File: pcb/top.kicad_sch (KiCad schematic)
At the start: 64 parts, among them J1 Conn_01x01, J10 Conn_01x01, J11 Conn_01x01, J2 Conn_01x01, J3 Conn_01x06, J4 Conn_01x01, J5 Conn_01x01, J6 Conn_01x01, J7 Conn_01x01, J8 Conn_01x01, J9 Conn_01x01, Q1 2N7002, Q2 2N7002, Q3 2N7002, Q4 2N7002, U1 L78L05_SOT89, U2 PIC12F629-ISN

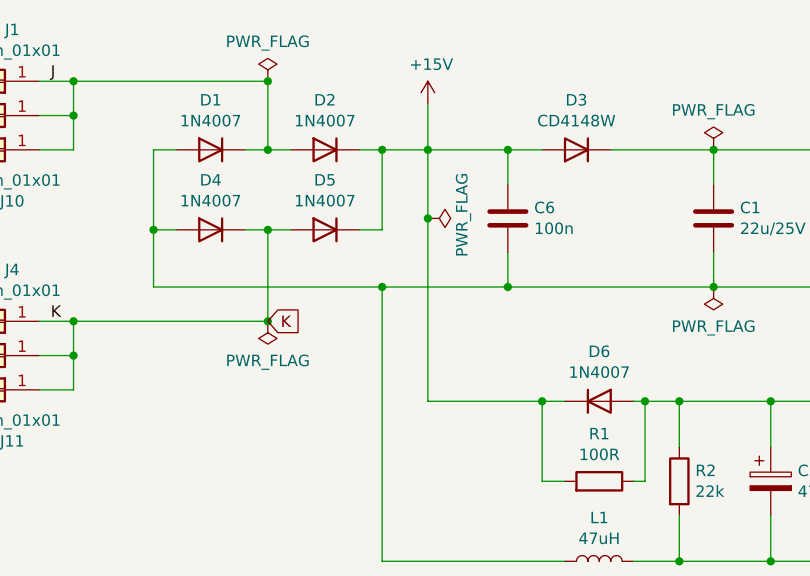
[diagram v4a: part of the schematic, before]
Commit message: Use schottky diodes on rectifier & capacitor.
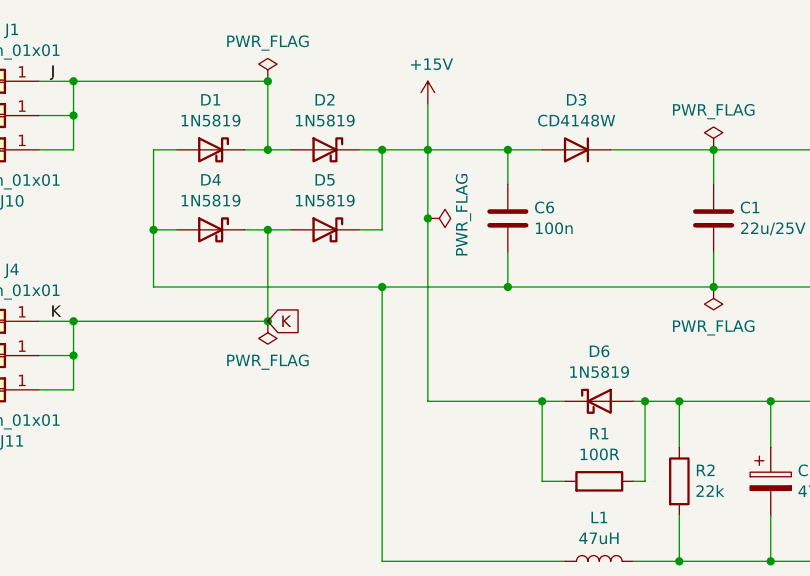
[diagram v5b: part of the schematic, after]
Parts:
- D1, D2, D4, D5, D6: value 1N4007 -> 1N5819; footprint Diode_SMD:D_SOD-123F -> Diode_SMD:D_SOD-123; symbol Diode:1N4007 -> Diode:1N5819; LCSC C64898 -> C8598
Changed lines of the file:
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@@
     (pin "8")
   )
-  (symbol (lib_id "Diode:1N4007") (at 59.69 45.72 0) (mirror y) (unit 1)
+  (symbol (lib_id "Diode:1N5819") (at 59.69 45.72 0) (mirror y) (unit 1)
     (in_bom yes) (on_board yes)
     (property "Reference" "D4" (id 0) (at 59.69 40.2082 0))
-    (property "Value" "1N4007" (id 1) (at 59.69 42.5196 0))
-    (property "Footprint" "Diode_SMD:D_SOD-123F" (id 2) (at 59.69 50.165 0)
-      (effects (font (size 1.27 1.27)) hide)
-    )
-    (property "Datasheet" "http://www.vishay.com/docs/88503/1n4001.pdf" (id 3) (at 59.69 45.72 0)
-      (effects (font (size 1.27 1.27)) hide)
-    )
-    (property "LCSC" "C64898" (id 4) (at 59.69 45.72 0)
-      (effects (font (size 1.27 1.27)) hide)
-    )
-    (pin "1")
-    (pin "2")
-  )
-  (symbol (lib_id "Diode:1N4007") (at 59.69 36.83 0) (mirror y) (unit 1)
+    (property "Value" "1N5819" (id 1) (at 59.69 42.5196 0))
+    (property "Footprint" "Diode_SMD:D_SOD-123" (id 2) (at 59.69 50.165 0)
+      (effects (font (size 1.27 1.27)) hide)
+    )
+    (property "Datasheet" "http://www.vishay.com/docs/88525/1n5817.pdf" (id 3) (at 59.69 45.72 0)
+      (effects (font (size 1.27 1.27)) hide)
+    )
+    (property "LCSC" "C8598" (id 4) (at 59.69 45.72 0)
+      (effects (font (size 1.27 1.27)) hide)
+    )
+    (pin "1")
+    (pin "2")
+  )
+  (symbol (lib_id "Diode:1N5819") (at 59.69 36.83 0) (mirror y) (unit 1)
     (in_bom yes) (on_board yes)
     (property "Reference" "D1" (id 0) (at 59.69 31.3182 0))
-    (property "Value" "1N4007" (id 1) (at 59.69 33.6296 0))
-    (property "Footprint" "Diode_SMD:D_SOD-123F" (id 2) (at 59.69 41.275 0)
-      (effects (font (size 1.27 1.27)) hide)
-    )
-    (property "Datasheet" "http://www.vishay.com/docs/88503/1n4001.pdf" (id 3) (at 59.69 36.83 0)
-      (effects (font (size 1.27 1.27)) hide)
-    )
-    (property "LCSC" "C64898" (id 4) (at 59.69 36.83 0)
-      (effects (font (size 1.27 1.27)) hide)
-    )
-    (pin "1")
-    (pin "2")
-  )
-  (symbol (lib_id "Diode:1N4007") (at 72.39 36.83 0) (mirror y) (unit 1)
+    (property "Value" "1N5819" (id 1) (at 59.69 33.6296 0))
+    (property "Footprint" "Diode_SMD:D_SOD-123" (id 2) (at 59.69 41.275 0)
+      (effects (font (size 1.27 1.27)) hide)
+    )
+    (property "Datasheet" "http://www.vishay.com/docs/88525/1n5817.pdf" (id 3) (at 59.69 36.83 0)
+      (effects (font (size 1.27 1.27)) hide)
+    )
+    (property "LCSC" "C8598" (id 4) (at 59.69 36.83 0)
+      (effects (font (size 1.27 1.27)) hide)
+    )
+    (pin "1")
+    (pin "2")
+  )
+  (symbol (lib_id "Diode:1N5819") (at 72.39 36.83 0) (mirror y) (unit 1)
     (in_bom yes) (on_board yes)
     (property "Reference" "D2" (id 0) (at 72.39 31.3182 0))
-    (property "Value" "1N4007" (id 1) (at 72.39 33.6296 0))
-    (property "Footprint" "Diode_SMD:D_SOD-123F" (id 2) (at 72.39 41.275 0)
-      (effects (font (size 1.27 1.27)) hide)
-    )
-    (property "Datasheet" "http://www.vishay.com/docs/88503/1n4001.pdf" (id 3) (at 72.39 36.83 0)
-      (effects (font (size 1.27 1.27)) hide)
-    )
-    (property "LCSC" "C64898" (id 4) (at 72.39 36.83 0)
-      (effects (font (size 1.27 1.27)) hide)
-    )
-    (pin "1")
-    (pin "2")
-  )
-  (symbol (lib_id "Diode:1N4007") (at 72.39 45.72 0) (mirror y) (unit 1)
+    (property "Value" "1N5819" (id 1) (at 72.39 33.6296 0))
+    (property "Footprint" "Diode_SMD:D_SOD-123" (id 2) (at 72.39 41.275 0)
+      (effects (font (size 1.27 1.27)) hide)
+    )
+    (property "Datasheet" "http://www.vishay.com/docs/88525/1n5817.pdf" (id 3) (at 72.39 36.83 0)
+      (effects (font (size 1.27 1.27)) hide)
+    )
+    (property "LCSC" "C8598" (id 4) (at 72.39 36.83 0)
+      (effects (font (size 1.27 1.27)) hide)
+    )
+    (pin "1")
+    (pin "2")
+  )
+  (symbol (lib_id "Diode:1N5819") (at 72.39 45.72 0) (mirror y) (unit 1)
     (in_bom yes) (on_board yes)
     (property "Reference" "D5" (id 0) (at 72.39 40.2082 0))
-    (property "Value" "1N4007" (id 1) (at 72.39 42.5196 0))
-    (property "Footprint" "Diode_SMD:D_SOD-123F" (id 2) (at 72.39 50.165 0)
-      (effects (font (size 1.27 1.27)) hide)
-    )
-    (property "Datasheet" "http://www.vishay.com/docs/88503/1n4001.pdf" (id 3) (at 72.39 45.72 0)
-      (effects (font (size 1.27 1.27)) hide)
-    )
-    (property "LCSC" "C64898" (id 4) (at 72.39 45.72 0)
+    (property "Value" "1N5819" (id 1) (at 72.39 42.5196 0))
+    (property "Footprint" "Diode_SMD:D_SOD-123" (id 2) (at 72.39 50.165 0)
+      (effects (font (size 1.27 1.27)) hide)
+    )
+    (property "Datasheet" "http://www.vishay.com/docs/88525/1n5817.pdf" (id 3) (at 72.39 45.72 0)
+      (effects (font (size 1.27 1.27)) hide)
+    )
+    (property "LCSC" "C8598" (id 4) (at 72.39 45.72 0)
       (effects (font (size 1.27 1.27)) hide)
     )
@@
     (pin "2")
   )
-  (symbol (lib_id "Diode:1N4007") (at 102.87 64.77 0) (unit 1)
+  (symbol (lib_id "Diode:1N5819") (at 102.87 64.77 0) (unit 1)
     (in_bom yes) (on_board yes)
     (property "Reference" "D6" (id 0) (at 102.87 59.2582 0))
-    (property "Value" "1N4007" (id 1) (at 102.87 61.5696 0))
-    (property "Footprint" "Diode_SMD:D_SOD-123F" (id 2) (at 102.87 69.215 0)
-      (effects (font (size 1.27 1.27)) hide)
-    )
-    (property "Datasheet" "http://www.vishay.com/docs/88503/1n4001.pdf" (id 3) (at 102.87 64.77 0)
-      (effects (font (size 1.27 1.27)) hide)
-    )
-    (property "LCSC" "C64898" (id 4) (at 102.87 64.77 0)
+    (property "Value" "1N5819" (id 1) (at 102.87 61.5696 0))
+    (property "Footprint" "Diode_SMD:D_SOD-123" (id 2) (at 102.87 69.215 0)
+      (effects (font (size 1.27 1.27)) hide)
+    )
+    (property "Datasheet" "http://www.vishay.com/docs/88525/1n5817.pdf" (id 3) (at 102.87 64.77 0)
+      (effects (font (size 1.27 1.27)) hide)
+    )
+    (property "LCSC" "C8598" (id 4) (at 102.87 64.77 0)
       (effects (font (size 1.27 1.27)) hide)
     )
@@
     )
     (path "/00000000-0000-0000-0000-000061c6e829"
-      (reference "D1") (unit 1) (value "1N4007") (footprint "Diode_SMD:D_SOD-123F")
+      (reference "D1") (unit 1) (value "1N5819") (footprint "Diode_SMD:D_SOD-123")
     )
     (path "/00000000-0000-0000-0000-000061c6ec88"
-      (reference "D2") (unit 1) (value "1N4007") (footprint "Diode_SMD:D_SOD-123F")
+      (reference "D2") (unit 1) (value "1N5819") (footprint "Diode_SMD:D_SOD-123")
     )
     (path "/00000000-0000-0000-0000-000061ed98d7"
@@
     )
     (path "/00000000-0000-0000-0000-000061c6deaf"
-      (reference "D4") (unit 1) (value "1N4007") (footprint "Diode_SMD:D_SOD-123F")
+      (reference "D4") (unit 1) (value "1N5819") (footprint "Diode_SMD:D_SOD-123")
     )
     (path "/00000000-0000-0000-0000-000061c6f498"
-      (reference "D5") (unit 1) (value "1N4007") (footprint "Diode_SMD:D_SOD-123F")
+      (reference "D5") (unit 1) (value "1N5819") (footprint "Diode_SMD:D_SOD-123")
     )
     (path "/00000000-0000-0000-0000-000061eeb281"
-      (reference "D6") (unit 1) (value "1N4007") (footprint "Diode_SMD:D_SOD-123F")
+      (reference "D6") (unit 1) (value "1N5819") (footprint "Diode_SMD:D_SOD-123")
     )
     (path "/00000000-0000-0000-0000-000061c7a55c"

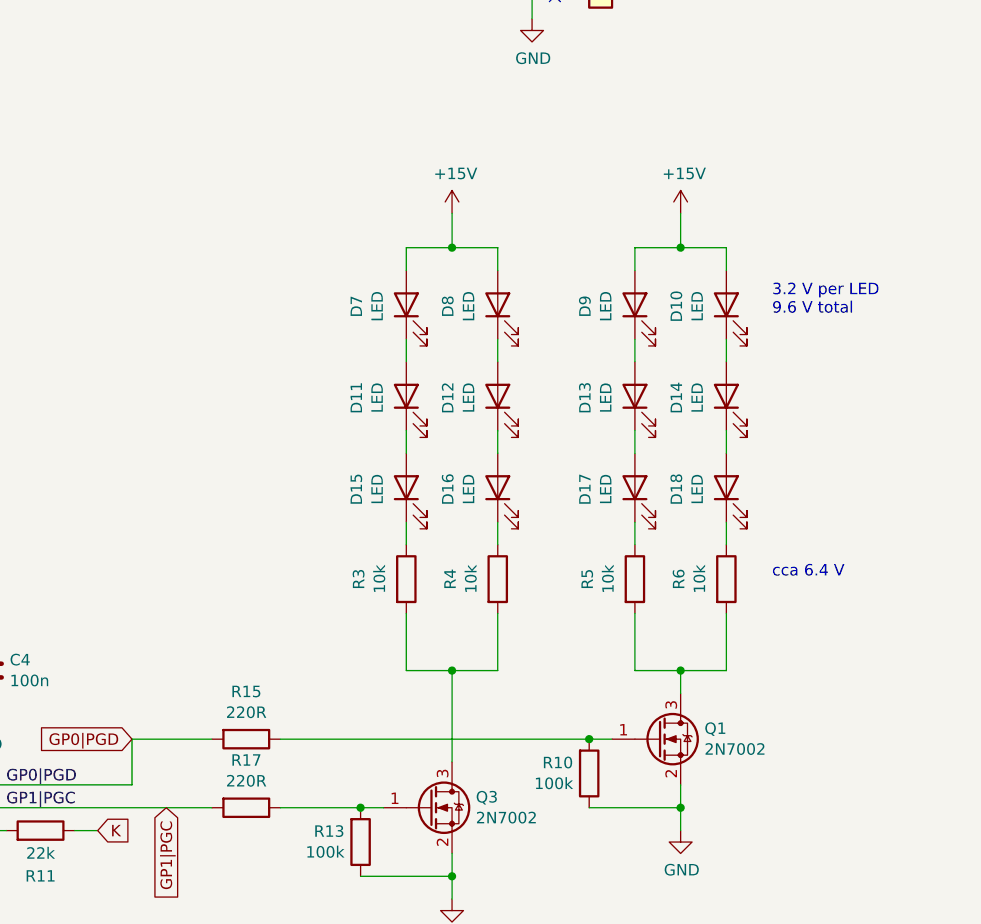
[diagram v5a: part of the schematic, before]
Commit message: Change order of LEDs to 2-2-2-2-2-2.
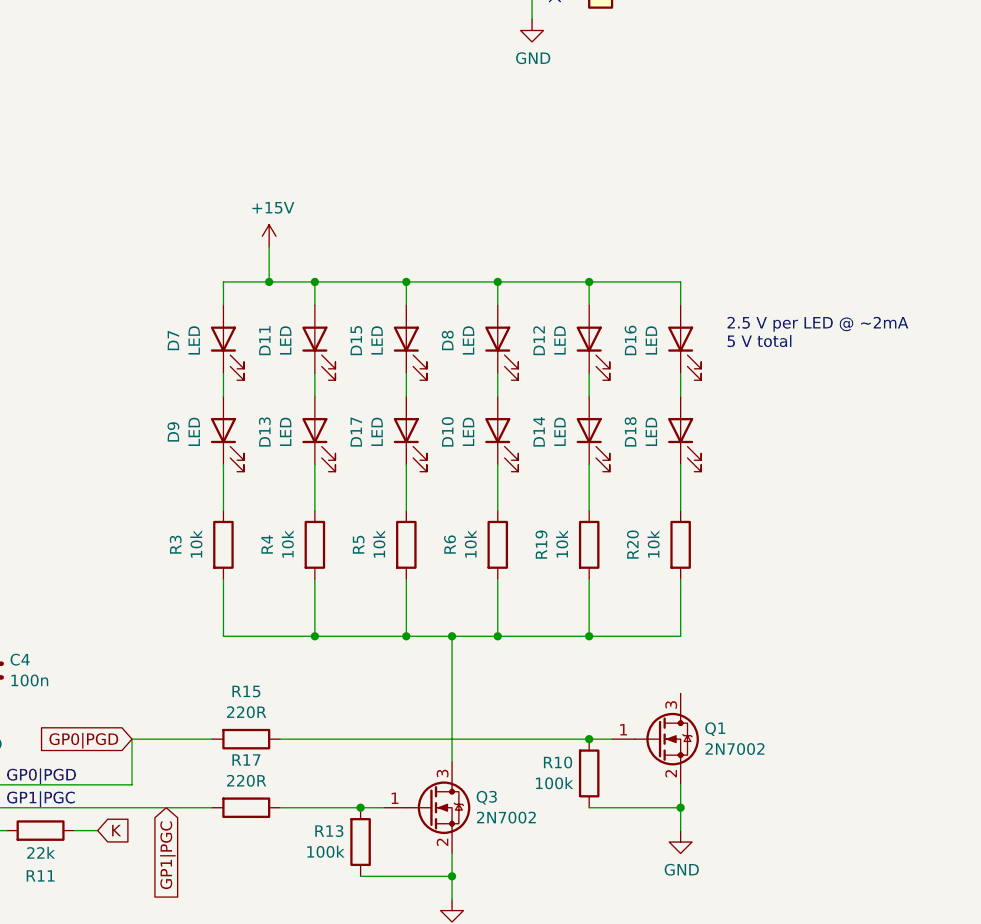
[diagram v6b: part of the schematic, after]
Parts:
- added R19, R20: 10k, Resistor_SMD:R_0805_2012Metric_Pad1.20x1.40mm_HandSolder, symbol Device:R
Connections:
- net +15V: now also D11.2 (A), D12.2 (A), D15.2 (A), D16.2 (A); no longer D10.2 (A), D9.2 (A)
- net at D7.1 (K): now also D9.2 (A); no longer D11.2 (A)
- net at D11.1 (K): now also D13.2 (A); no longer D15.2 (A)
- net at D15.1 (K): now also D17.2 (A); no longer R3.1
- net at D8.1 (K): now also D10.2 (A); no longer D12.2 (A)
- net at D12.1 (K): now also D14.2 (A); no longer D16.2 (A)
- net at D16.1 (K): now also D18.2 (A); no longer R4.1
- net at D9.1 (K): now also R3.1; no longer D13.2 (A)
- net at D13.1 (K): now also R4.1; no longer D17.2 (A)
- net at D10.1 (K): now also R6.1; no longer D14.2 (A)
- net at D14.1 (K): now also R19.1; no longer D18.2 (A)
- net at D18.1 (K): now also R20.1; no longer R6.1
- net at R5.2, R6.2: now also Q3.3 (D), R3.2, R4.2, R19.2, R20.2; no longer Q1.3 (D)
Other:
- note added: "2.5 V per LED @ ~2mA 5 V total"
- note removed: "3.2 V per LED 9.6 V total"
- note removed: "cca 6.4 V"
- moved on the sheet: D10, D11, D12, D13, D14, D15, D16, D17, D18, D7, D8, D9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

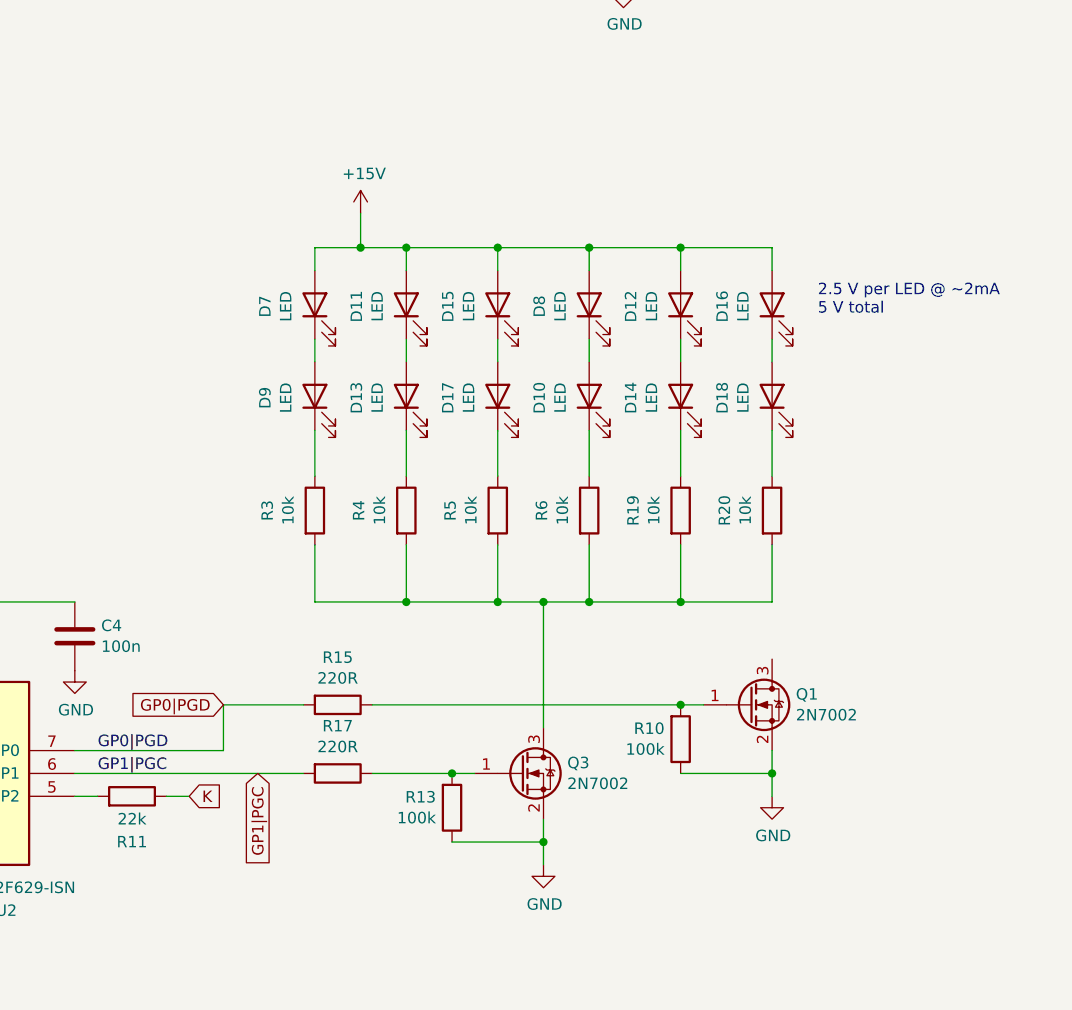
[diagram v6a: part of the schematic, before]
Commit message: Add load resistor for CV reading.
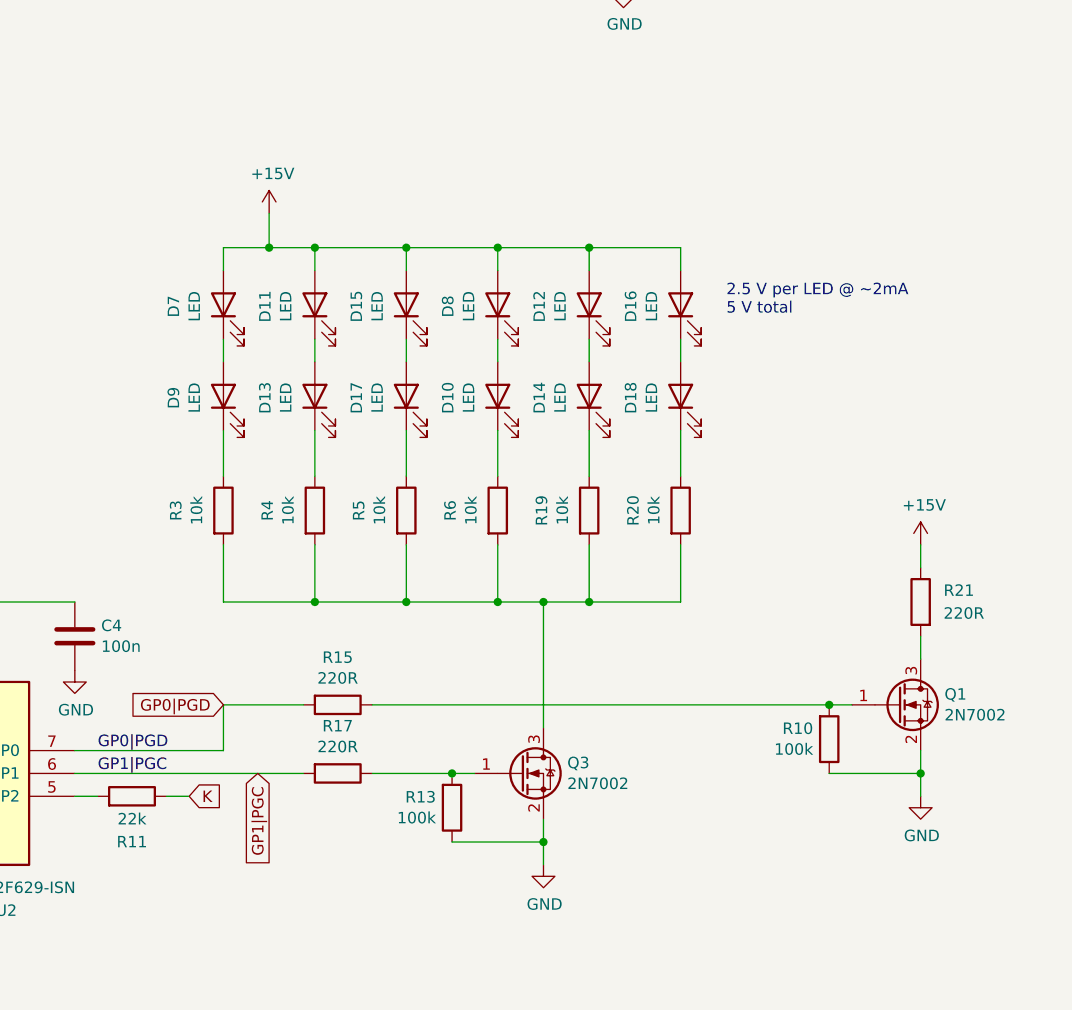
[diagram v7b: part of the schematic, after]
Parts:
- added R21: 220R, Resistor_SMD:R_2512_6332Metric_Pad1.40x3.35mm_HandSolder, symbol Device:R
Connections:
- net +15V: now also R21.1
- net at Q1.3 (D): now also R21.2
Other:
- moved on the sheet: D10, D11, D12, D13, D14, D15, D16, D17, D18, D7, D8, D9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
